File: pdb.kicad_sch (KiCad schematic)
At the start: 33 parts, among them J1 Amass Elec AS150UPW(2+4), J10 BOOMELE 4.2-2*2AW, J11 BOOMELE 4.2-2*3AW, J12 BOOMELE 4.2-2*4AW, J13 BOOMELE 4.2-2*4AW, J14 BOOMELE 4.2-2*3AW, J15 BOOMELE 4.2-2*3AW, J16 BOOMELE 4.2-2*4AW, J17 BOOMELE 4.2-2*4AW, J18 BOOMELE 4.2-2*3AW, J19 BOOMELE 4.2-2*2AW, J2 BOOMELE 4.2-2*3AW, J20 BOOMELE 4.2-2*4AW, J21 BOOMELE 4.2-2*4AW, J22 BOOMELE 4.2-2*2AW, J23 BOOMELE 4.2-2*4AW, J3 BOOMELE 4.2-2*4AW, J4 BOOMELE 4.2-2*3AW, J5 BOOMELE 4.2-2*3AW, J6 MOLEX 39301240, J7 BOOMELE 4.2-2*3AW, J8 BOOMELE 4.2-2*3AW, J9 BOOMELE 4.2-2*2AW

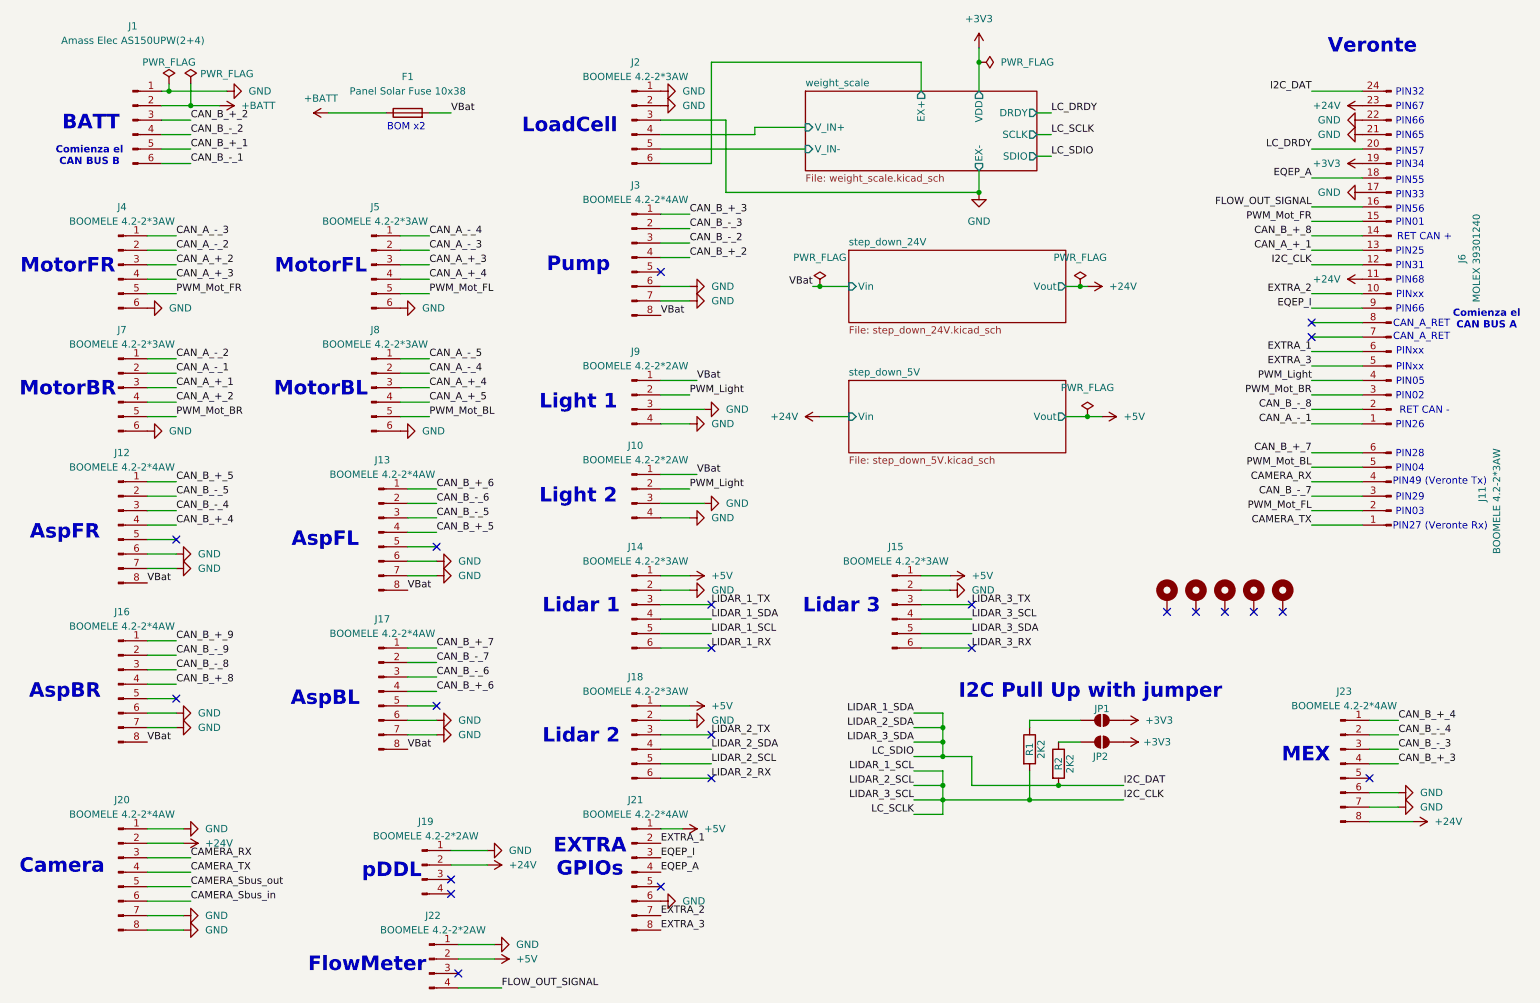
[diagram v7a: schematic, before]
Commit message: Agregado los testpoint, falta leds indicadores y serigrafia y cerramos
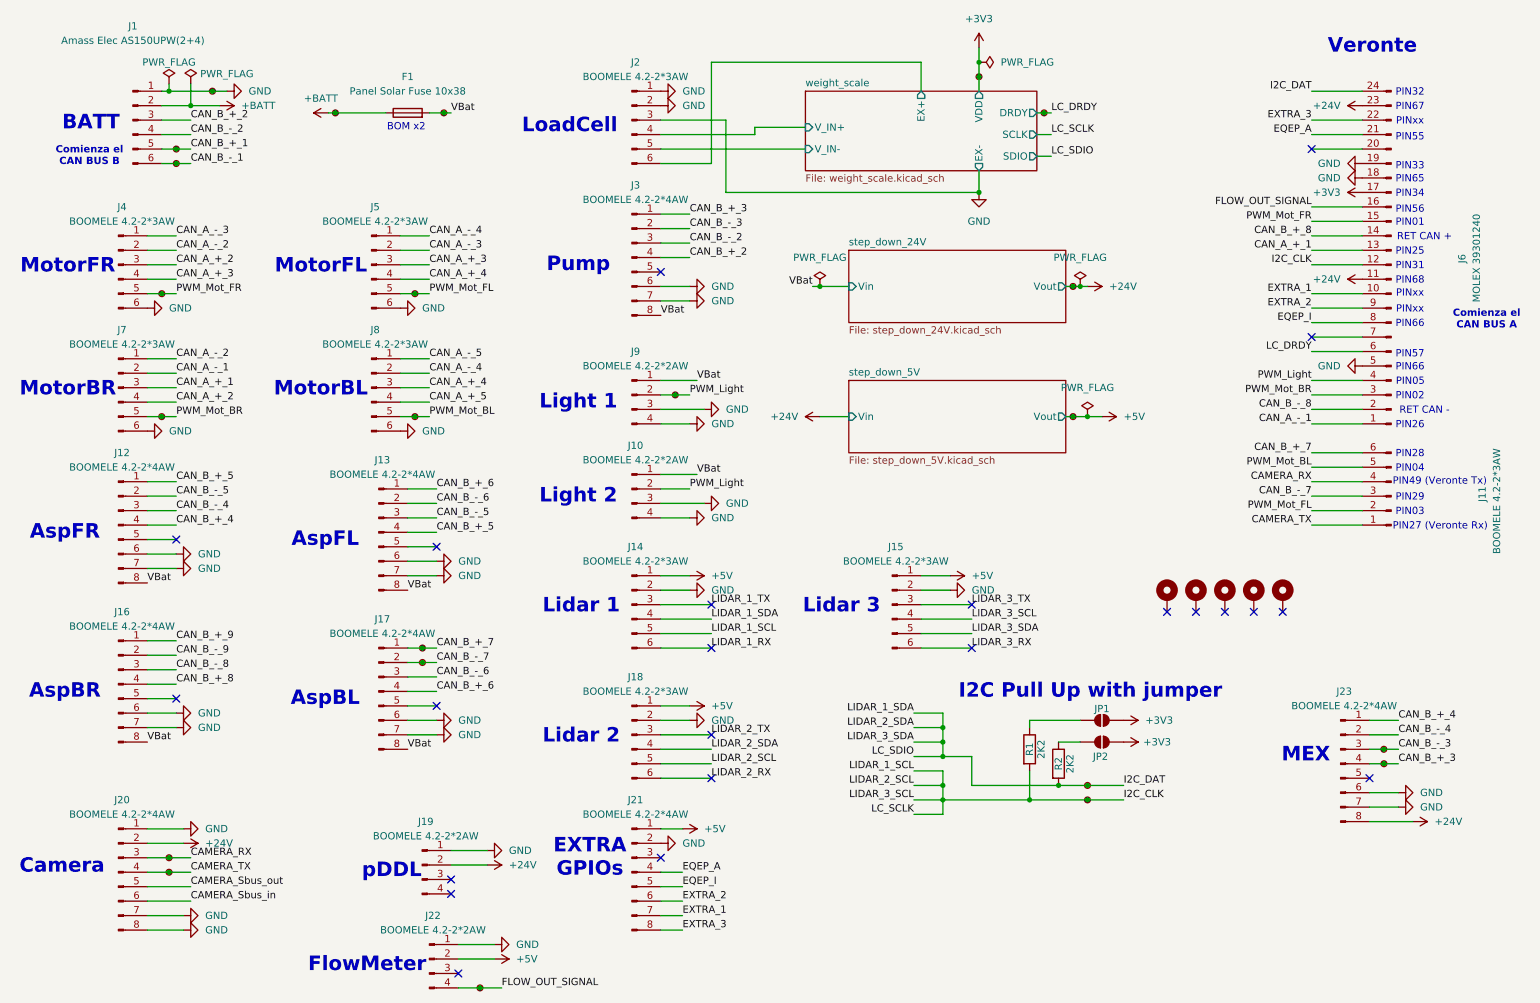
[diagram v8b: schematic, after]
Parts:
- added TP1: +BATT, 0_ZA_Lib:TestPoint_Pad_D2.0mm_silk_value, symbol Connector:TestPoint_Small
- added TP12: CAM_RX, 0_ZA_Lib:TestPoint_Pad_D2.0mm_silk_value, symbol Connector:TestPoint_Small
- added TP13: CAM_TX, 0_ZA_Lib:TestPoint_Pad_D2.0mm_silk_value, symbol Connector:TestPoint_Small
- added TP14: PWM_MOT_FR, 0_ZA_Lib:TestPoint_Pad_D2.0mm_silk_value, symbol Connector:TestPoint_Small
- added TP15: PWM_MOT_BR, 0_ZA_Lib:TestPoint_Pad_D2.0mm_silk_value, symbol Connector:TestPoint_Small
- added TP16: PWM_MOT_BL, 0_ZA_Lib:TestPoint_Pad_D2.0mm_silk_value, symbol Connector:TestPoint_Small
- added TP17: PWM_MOT_FL, 0_ZA_Lib:TestPoint_Pad_D2.0mm_silk_value, symbol Connector:TestPoint_Small
- added TP18: FLOW_S, 0_ZA_Lib:TestPoint_Pad_D2.0mm_silk_value, symbol Connector:TestPoint_Small
- added TP19: PWM_LIGHT, 0_ZA_Lib:TestPoint_Pad_D2.0mm_silk_value, symbol Connector:TestPoint_Small
- added TP2: VBat, 0_ZA_Lib:TestPoint_Pad_D2.0mm_silk_value, symbol Connector:TestPoint_Small
- added TP20: +24V, 0_ZA_Lib:TestPoint_Pad_D2.0mm_silk_value, symbol Connector:TestPoint_Small
- added TP21: +5V, 0_ZA_Lib:TestPoint_Pad_D2.0mm_silk_value, symbol Connector:TestPoint_Small
- added TP22: +3V3, 0_ZA_Lib:TestPoint_Pad_D2.0mm_silk_value, symbol Connector:TestPoint_Small
- added TP23: I2C_DAT, 0_ZA_Lib:TestPoint_Pad_D2.0mm_silk_value, symbol Connector:TestPoint_Small
- added TP24: I2C_CLK, 0_ZA_Lib:TestPoint_Pad_D2.0mm_silk_value, symbol Connector:TestPoint_Small
- added TP27: LC_DRDY, 0_ZA_Lib:TestPoint_Pad_D2.0mm_silk_value, symbol Connector:TestPoint_Small
- added TP28: CAN_B_-_3, 0_ZA_Lib:TestPoint_Pad_D2.0mm_silk_value, symbol Connector:TestPoint_Small
- added TP29: CAN_B_+_3, 0_ZA_Lib:TestPoint_Pad_D2.0mm_silk_value, symbol Connector:TestPoint_Small
- added TP3: GND, 0_ZA_Lib:TestPoint_Pad_D2.0mm_silk_value, symbol Connector:TestPoint_Small
- added TP4: CAN_B_+_1, 0_ZA_Lib:TestPoint_Pad_D2.0mm_silk_value, symbol Connector:TestPoint_Small
- added TP5: CAN_B_-_1, 0_ZA_Lib:TestPoint_Pad_D2.0mm_silk_value, symbol Connector:TestPoint_Small
- added TP8: CAN_B_+_7, 0_ZA_Lib:TestPoint_Pad_D2.0mm_silk_value, symbol Connector:TestPoint_Small
- added TP9: CAN_B_-_7, 0_ZA_Lib:TestPoint_Pad_D2.0mm_silk_value, symbol Connector:TestPoint_Small
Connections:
- net +24V: now also TP20.1
- net +3V3: now also J6.17 (Pin_17), TP22.1; no longer J6.19 (Pin_19)
- net +5V: now also TP21.1
- net +BATT: now also TP1.1
- net CAMERA_RX: now also TP12.1
- net CAMERA_TX: now also TP13.1
- net CAN_B_+_1: now also TP4.1
- net CAN_B_+_3: now also TP29.1
- net CAN_B_+_7: now also TP8.1
- net CAN_B_-_1: now also TP5.1
- net CAN_B_-_3: now also TP28.1
- net CAN_B_-_7: now also TP9.1
- net EQEP_A: now also J6.21 (Pin_21); no longer J6.18 (Pin_18)
- net EQEP_I: now also J21.5 (Pin_5), J6.8 (Pin_8); no longer J21.3 (Pin_3), J6.9 (Pin_9)
- net EXTRA_1: now also J21.7 (Pin_7), J6.10 (Pin_10); no longer J21.2 (Pin_2), J6.6 (Pin_6)
- net EXTRA_2: now also J21.6 (Pin_6), J6.9 (Pin_9); no longer J21.7 (Pin_7), J6.10 (Pin_10)
- net EXTRA_3: now also J6.22 (Pin_22); no longer J6.5 (Pin_5)
- net FLOW_OUT_SIGNAL: now also TP18.1
- net GND: now also J21.2 (Pin_2), J6.18 (Pin_18), J6.19 (Pin_19), J6.5 (Pin_5), TP3.1; no longer J21.6 (Pin_6), J6.17 (Pin_17), J6.21 (Pin_21), J6.22 (Pin_22)
- net I2C_CLK: now also TP24.1
- net I2C_DAT: now also TP23.1
- net LC_DRDY: now also J6.6 (Pin_6), TP27.1; no longer J6.20 (Pin_20)
- net PWM_Light: now also TP19.1
- net PWM_Mot_BL: now also TP16.1
- net PWM_Mot_BR: now also TP15.1
- net PWM_Mot_FL: now also TP17.1
- net PWM_Mot_FR: now also TP14.1
- net VBat: now also TP2.1
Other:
- note removed: "CAN_A_RET"
